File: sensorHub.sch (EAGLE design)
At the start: 3 parts

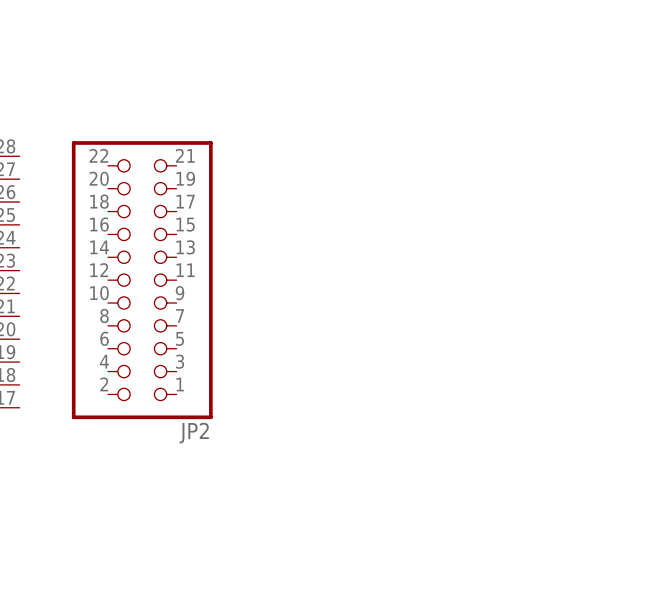
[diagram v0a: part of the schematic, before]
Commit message: Adds the lm2577 and two pull up resistors to the shematic
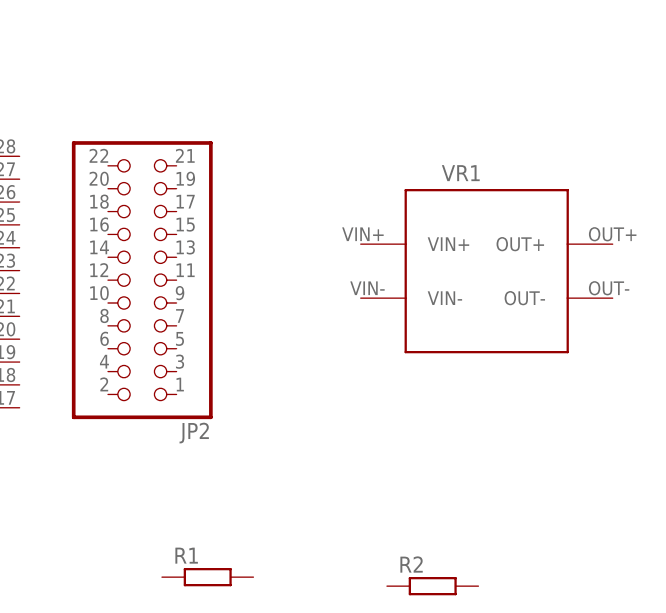
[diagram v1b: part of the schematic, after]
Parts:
- added R1, R2: (no value), resistor:R-EU_0207/10
- added VR1: (no value), lm2577_module:MT3608THROUGH_HOLE
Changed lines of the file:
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@@
 <part name="JP1" library="pinhead" library_urn="urn:adsk.eagle:library:325" deviceset="PINHD-2X16" device="" package3d_urn="urn:adsk.eagle:package:22431/2"/>
 <part name="JP2" library="pinhead" library_urn="urn:adsk.eagle:library:325" deviceset="PINHD-2X11" device="" package3d_urn="urn:adsk.eagle:package:22419/2"/>
+<part name="VR1" library="lm2577_module" deviceset="MT3608" device="THROUGH_HOLE"/>
+<part name="R1" library="resistor" library_urn="urn:adsk.eagle:library:348" deviceset="R-EU_" device="0207/10" package3d_urn="urn:adsk.eagle:package:25939/1"/>
+<part name="R2" library="resistor" library_urn="urn:adsk.eagle:library:348" deviceset="R-EU_" device="0207/10" package3d_urn="urn:adsk.eagle:package:25939/1"/>
 </parts>
 <sheets>
@@
 <attribute name="VALUE" x="85.35" y="117.78" size="1.778" layer="96" rot="R180"/>
 </instance>
+<instance part="VR1" gate="G$1" x="116" y="101" smashed="yes">
+<attribute name="NAME" x="111" y="111" size="1.778" layer="95"/>
+<attribute name="VALUE" x="111" y="89" size="1.778" layer="96"/>
+</instance>
+<instance part="R1" gate="G$1" x="85" y="67" smashed="yes">
+<attribute name="NAME" x="81.19" y="68.4986" size="1.778" layer="95"/>
+<attribute name="VALUE" x="81.19" y="63.698" size="1.778" layer="96"/>
+</instance>
+<instance part="R2" gate="G$1" x="110" y="66" smashed="yes">
+<attribute name="NAME" x="106.19" y="67.4986" size="1.778" layer="95"/>
+<attribute name="VALUE" x="106.19" y="62.698" size="1.778" layer="96"/>
+</instance>
 </instances>

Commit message: Adds connector pins for the sensors to the schematic
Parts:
- added J1, J2: (no value), SparkFun-Connectors:CONN_03SCREW
- added J3, J4, J5: (no value), SparkFun-Connectors:CONN_04SCREW
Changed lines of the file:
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@@
 <layer number="112" name="tSilk" color="7" fill="1" visible="no" active="yes"/>
 <layer number="113" name="ReferenceLS" color="7" fill="1" visible="no" active="no"/>
+<layer number="114" name="Badge_Outline" color="7" fill="1" visible="yes" active="yes"/>
+<layer number="115" name="ReferenceISLANDS" color="7" fill="1" visible="yes" active="yes"/>
 <layer number="116" name="Patch_BOT" color="9" fill="4" visible="no" active="yes"/>
 <layer number="118" name="Rect_Pads" color="7" fill="1" visible="no" active="no"/>
@@
 <part name="R1" library="resistor" library_urn="urn:adsk.eagle:library:348" deviceset="R-EU_" device="0207/10" package3d_urn="urn:adsk.eagle:package:25939/1"/>
 <part name="R2" library="resistor" library_urn="urn:adsk.eagle:library:348" deviceset="R-EU_" device="0207/10" package3d_urn="urn:adsk.eagle:package:25939/1"/>
+<part name="J1" library="SparkFun-Connectors" deviceset="CONN_03" device="SCREW"/>
+<part name="J2" library="SparkFun-Connectors" deviceset="CONN_03" device="SCREW"/>
+<part name="J3" library="SparkFun-Connectors" deviceset="CONN_04" device="SCREW"/>
+<part name="J4" library="SparkFun-Connectors" deviceset="CONN_04" device="SCREW"/>
+<part name="J5" library="SparkFun-Connectors" deviceset="CONN_04" device="SCREW"/>
 </parts>
 <sheets>
@@
 <attribute name="VALUE" x="106.19" y="62.698" size="1.778" layer="96"/>
 </instance>
+<instance part="J1" gate="J$1" x="3" y="65" smashed="yes">
+<attribute name="VALUE" x="0.46" y="57.634" size="1.778" layer="96" font="vector"/>
+<attribute name="NAME" x="0.46" y="70.588" size="1.778" layer="95" font="vector"/>
+</instance>
+<instance part="J2" gate="J$1" x="23" y="64" smashed="yes">
+<attribute name="VALUE" x="20.46" y="56.634" size="1.778" layer="96" font="vector"/>
+<attribute name="NAME" x="20.46" y="69.588" size="1.778" layer="95" font="vector"/>
+</instance>
+<instance part="J3" gate="G$1" x="46" y="62" smashed="yes">
+<attribute name="VALUE" x="40.92" y="54.634" size="1.778" layer="96" font="vector"/>
+<attribute name="NAME" x="40.92" y="70.128" size="1.778" layer="95" font="vector"/>
+</instance>
+<instance part="J4" gate="G$1" x="46" y="43" smashed="yes">
+<attribute name="VALUE" x="40.92" y="35.634" size="1.778" layer="96" font="vector"/>
+<attribute name="NAME" x="40.92" y="51.128" size="1.778" layer="95" font="vector"/>
+</instance>
+<instance part="J5" gate="G$1" x="69" y="43" smashed="yes">
+<attribute name="VALUE" x="63.92" y="35.634" size="1.778" layer="96" font="vector"/>
+<attribute name="NAME" x="63.92" y="51.128" size="1.778" layer="95" font="vector"/>
+</instance>
 </instances>

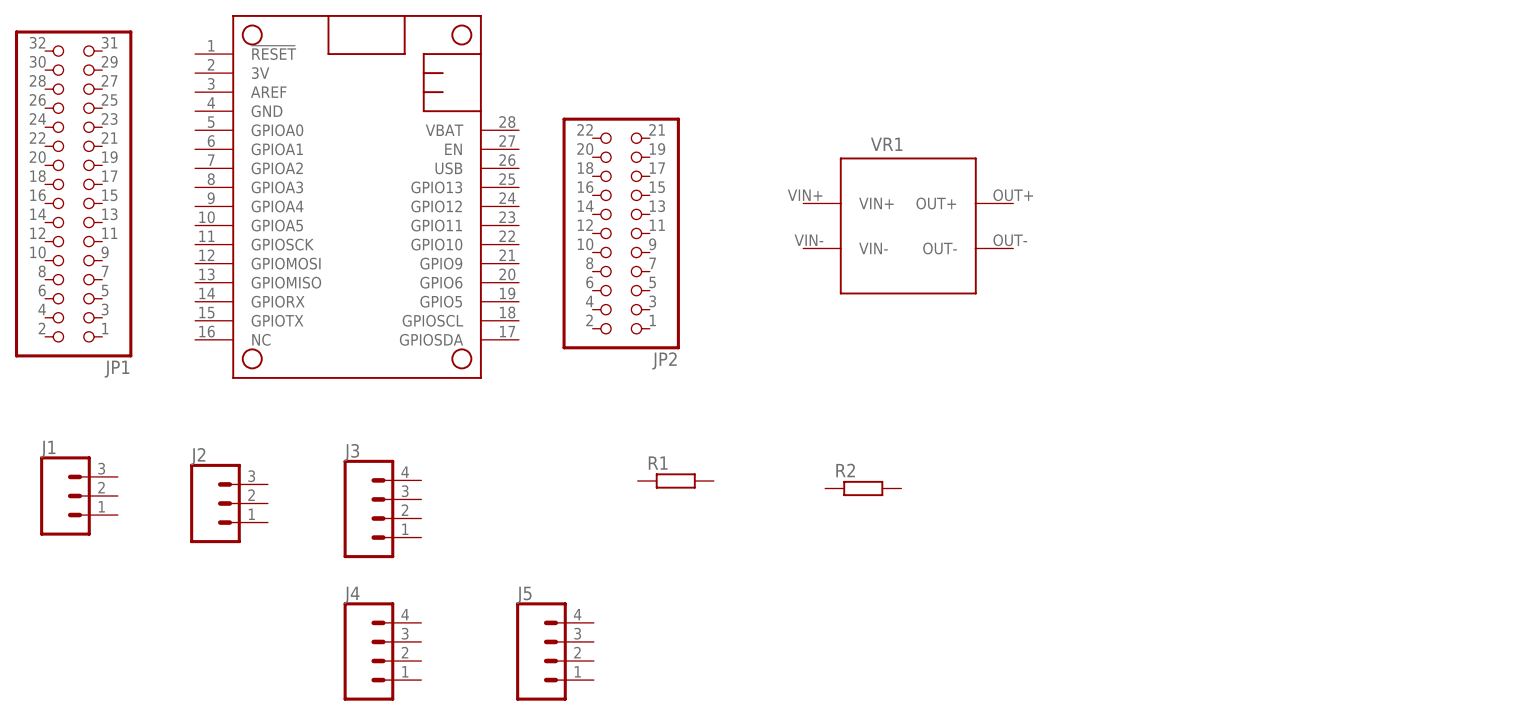
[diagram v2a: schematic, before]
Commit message: Completes connections in the schematic
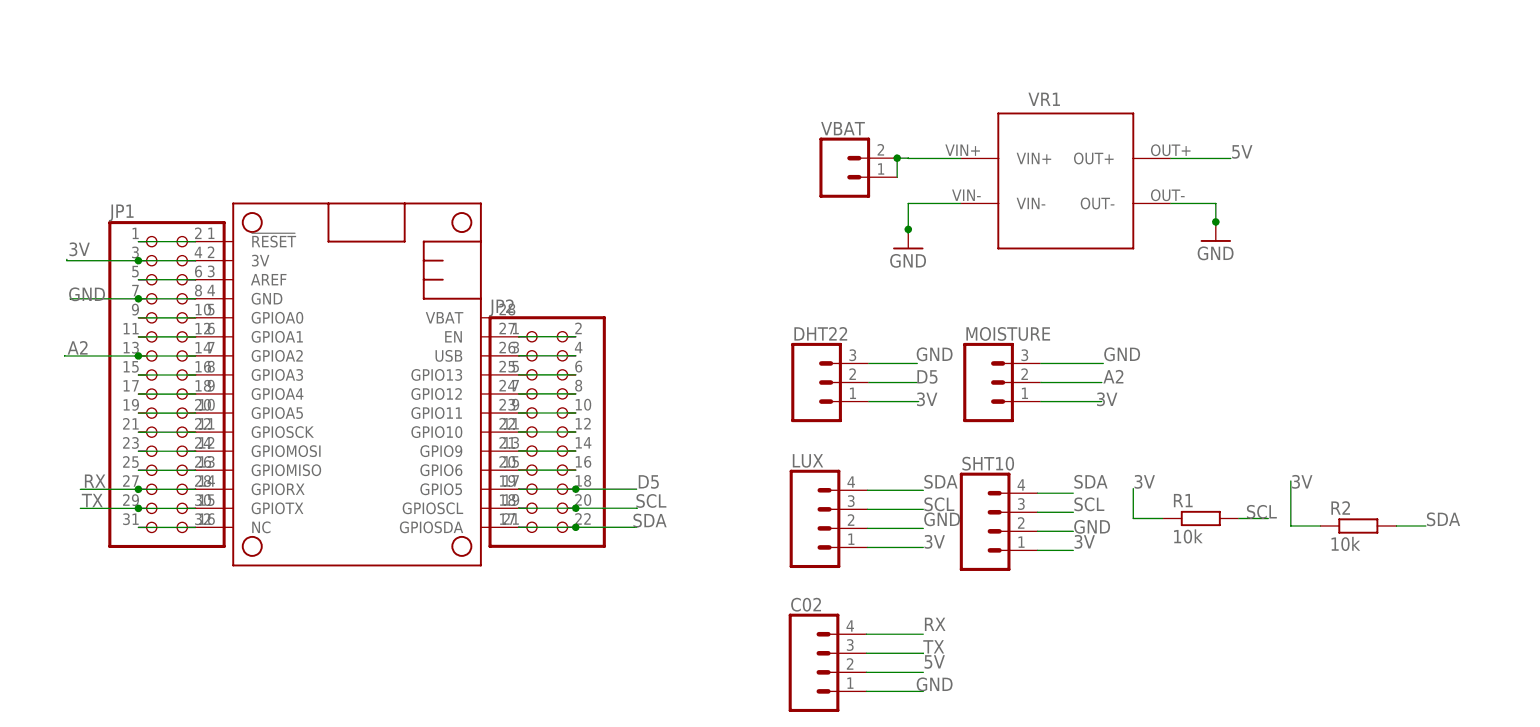
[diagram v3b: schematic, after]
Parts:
- removed J1, J2: (no value), SparkFun-Connectors:CONN_03SCREW
- removed J3, J4, J5: (no value), SparkFun-Connectors:CONN_04SCREW
- added C02, LUX, SHT10: (no value), SparkFun-Connectors:CONN_04SCREW
- added DHT22, MOISTURE: (no value), SparkFun-Connectors:CONN_03SCREW
- added VBAT: (no value), SparkFun-Connectors:CONN_02
- R1, R2: value (none) -> 10k
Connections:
- new net 3V: DHT22.1, JP1.3, JP1.4, LUX.1, MOISTURE.1, R1.1, R2.1, SHT10.1
- new net 5V: C02.2, VR1.OUT+
- new net A2: JP1.13, JP1.14, MOISTURE.2
- new net D5: DHT22.2, JP2.17, JP2.18
- new net GND: C02.1, DHT22.3, JP1.7, JP1.8, LUX.2, MOISTURE.3, SHT10.2, VR1.OUT-, VR1.VIN-
- new net N$1: JP1.1, JP1.2
- new net N$10: JP1.19, JP1.20
- new net N$11: JP1.21, JP1.22
- new net N$12: JP1.23, JP1.24
- new net N$13: JP1.25, JP1.26
- new net N$16: JP1.31, JP1.32
- new net N$17: JP2.1, JP2.2
- new net N$18: JP2.3, JP2.4
- new net N$19: JP2.5, JP2.6
- new net N$20: JP2.7, JP2.8
- new net N$21: JP2.10, JP2.9
- new net N$22: JP2.11, JP2.12
- new net N$23: JP2.13, JP2.14
- new net N$24: JP2.15, JP2.16
- new net N$27: VBAT.1, VBAT.2, VR1.VIN+
- new net N$3: JP1.5, JP1.6
- new net N$5: JP1.10, JP1.9
- new net N$6: JP1.11, JP1.12
- new net N$8: JP1.15, JP1.16
- new net N$9: JP1.17, JP1.18
- new net RX: C02.4, JP1.27, JP1.28
- new net SCL: JP2.19, JP2.20, LUX.3, R1.2, SHT10.3
- new net SDA: JP2.21, JP2.22, LUX.4, R2.2, SHT10.4
- new net TX: C02.3, JP1.29, JP1.30
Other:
- moved on the sheet: JP1, JP2, R1, R2, VR1

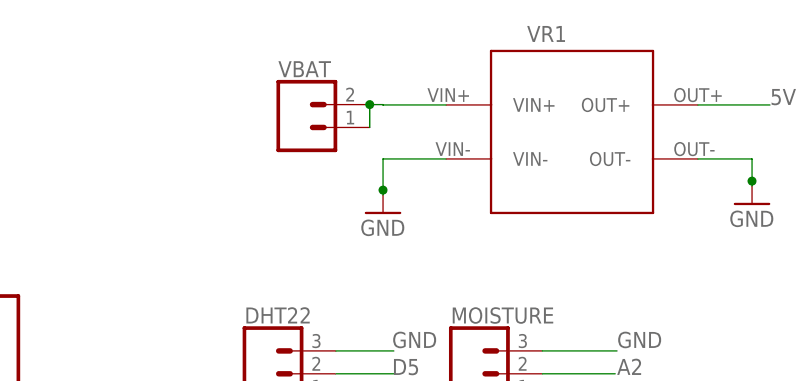
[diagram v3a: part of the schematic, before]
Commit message: Places components in pcb brd layout
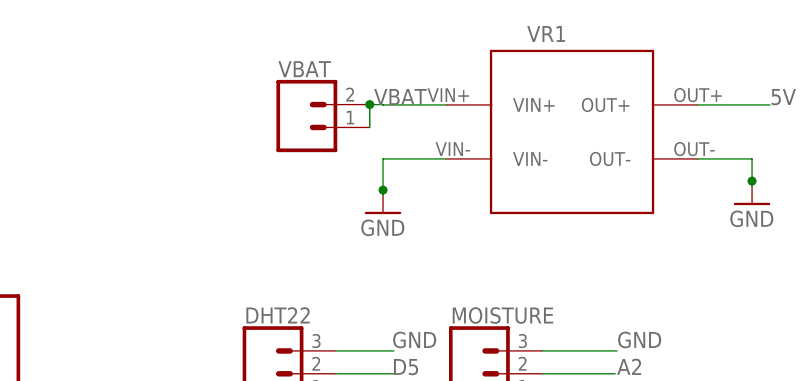
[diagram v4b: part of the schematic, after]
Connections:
- net N$27 renamed VBAT
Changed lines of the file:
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@@
 </segment>
 </net>
-<net name="N$27" class="0">
+<net name="VBAT" class="0">
 <segment>
 <pinref part="VR1" gate="G$1" pin="VIN+"/>
@@
 <wire x1="114.52" y1="107.5" x2="114.52" y2="110.04" width="0.1524" layer="91"/>
 <junction x="114.52" y="110.04"/>
+<label x="115" y="110" size="1.778" layer="95"/>
 </segment>
 </net>
@@
 </sheet>
 </sheets>
+<errors>
+</errors>
 </schematic>
 </drawing>

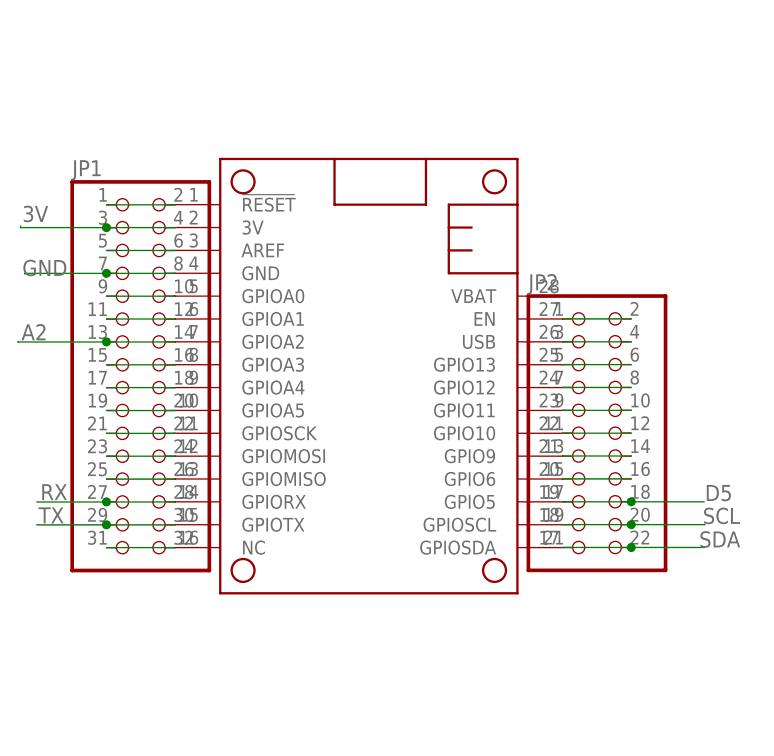
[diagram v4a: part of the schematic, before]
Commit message: Deletes the feather board
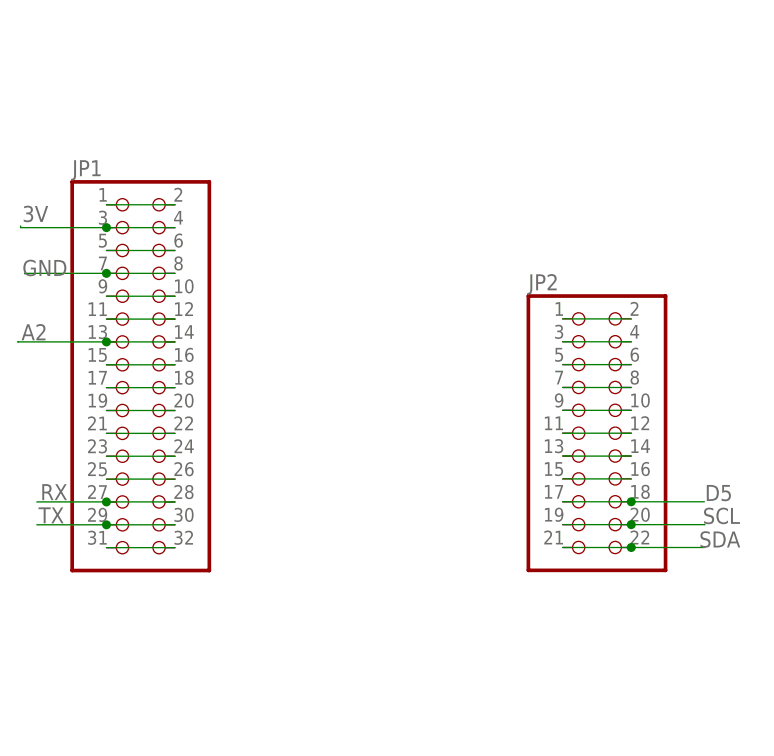
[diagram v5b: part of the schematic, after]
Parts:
- removed MS1: FEATHERWING, adafruit:FEATHERWING
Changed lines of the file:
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@@
 <setting verticaltext="up"/>
 </settings>
-<grid distance="1" unitdist="mm" unit="mm" style="dots" multiple="1" display="yes" altdistance="1" altunitdist="mm" altunit="mm"/>
+<grid distance="0.1" unitdist="inch" unit="inch" style="lines" multiple="1" display="no" altdistance="0.01" altunitdist="inch" altunit="inch"/>
 <layers>
 <layer number="1" name="Top" color="4" fill="1" visible="no" active="no"/>
@@
 </classes>
 <parts>
-<part name="MS1" library="adafruit" deviceset="FEATHERWING" device=""/>
 <part name="JP1" library="pinhead" library_urn="urn:adsk.eagle:library:325" deviceset="PINHD-2X16" device="" package3d_urn="urn:adsk.eagle:package:22431/2"/>
 <part name="JP2" library="pinhead" library_urn="urn:adsk.eagle:library:325" deviceset="PINHD-2X11" device="" package3d_urn="urn:adsk.eagle:package:22419/2"/>
@@
 </plain>
 <instances>
-<instance part="MS1" gate="G$1" x="26" y="104" smashed="yes" rot="R270"/>
 <instance part="JP1" gate="A" x="15.9" y="81.13" smashed="yes">
 <attribute name="NAME" x="9.55" y="102.085" size="1.778" layer="95"/>
